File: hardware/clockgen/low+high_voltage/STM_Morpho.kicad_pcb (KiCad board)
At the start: 4 copper layers, 70 x 95.8 mm, 32 parts, among them CN10 Conn_02x19_Odd_Even, CN7 Conn_02x19_Odd_Even, J1 Conn_02x20_Odd_Even, J2 Conn_02x20_Odd_Even, U1 74ALVC164245DLG4, U10 CD40109BNSR, U2 74ALVC164245DLG4, U3 CD40109BNSR, U4 CD40109BNSR, U5 CD40109BNSR, U6 CD40109BNSR, U7 CD40109BNSR, U8 CD40109BNSR, U9 CD40109BNSR

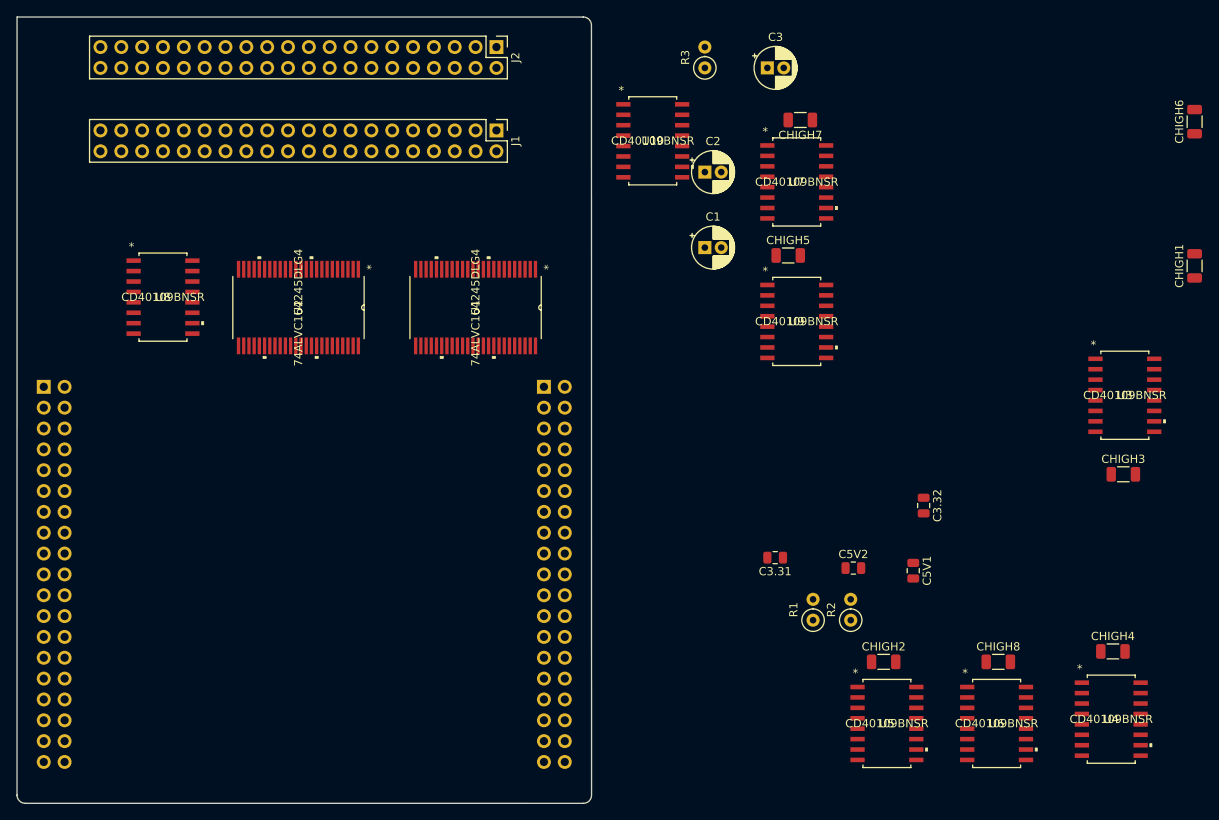
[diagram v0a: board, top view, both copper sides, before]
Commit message: Two PCBs are routed
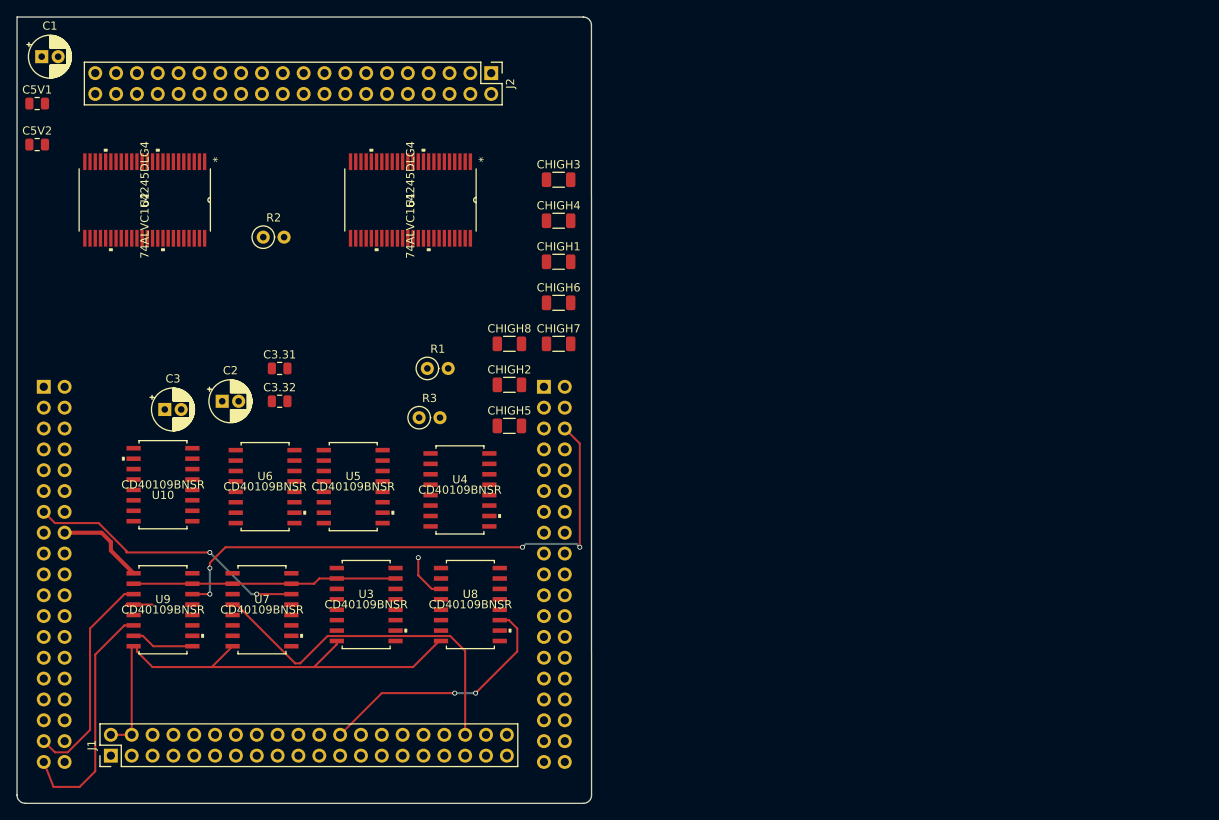
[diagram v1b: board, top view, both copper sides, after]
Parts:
- J1, J2: value Conn_02x20_Odd_Even -> Conn_02x20_Counter_Clockwise
- moved C5V1 121.0 mm to (132.4, 36.7), turned to 0 degrees
- moved C5V2 112.1 mm to (132.4, 41.7)
- moved U3 95.9 mm to (172.5, 97.8)
- moved U6 93.7 mm to (160.2, 83.4)
- moved J1 89.5 mm to (141.4, 116.2), turned to 90 degrees
- moved CHIGH4 85.6 mm to (196.0, 51.0)
- moved R2 85.5 mm to (160.0, 53.0), turned to 0 degrees
- moved U9 84.9 mm to (147.8, 98.4)
- moved C3 84.4 mm to (148.0, 74.0)
- moved U4 84.1 mm to (184.0, 83.8)
- moved C1 84.1 mm to (133.0, 31.0)
- moved U7 83.5 mm to (159.8, 98.4)
- moved CHIGH6 80.6 mm to (196.0, 61.0), turned to 0 degrees
- moved C3.32 79.5 mm to (162.0, 73.0), turned to 0 degrees
- moved CHIGH3 77.6 mm to (196.0, 46.0)
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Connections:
- CN10 pad 16: (no net) -> /PB12
- CN10 pad 22: (no net) -> /PB2
- CN10 pad 24: (no net) -> /PB1
- CN10 pad 26: (no net) -> /PB15
- CN10 pad 27: (no net) -> /PB4
- CN10 pad 28: (no net) -> /PB14
- CN10 pad 30: (no net) -> /PB13
- CN10 pad 31: (no net) -> /PB3
- CN10 pad 32: (no net) -> /AGND
- CN10 pad 7: (no net) -> /AVDD
- CN10 pad 8: (no net) -> /U5V
- CN7 pad 12: (no net) -> /IOREF
- CN7 pad 14: (no net) -> /RESET
- CN7 pad 2: (no net) -> /PC11
- CN7 pad 21: (no net) -> /PB7
- CN7 pad 23: (no net) -> /PC13
- CN7 pad 24: (no net) -> /VIN
- CN7 pad 25: (no net) -> /PC14
- CN7 pad 27: (no net) -> /PC15
- CN7 pad 29: (no net) -> /PH0
- CN7 pad 3: (no net) -> /PC12
- CN7 pad 31: (no net) -> /PH1
- CN7 pad 33: (no net) -> /VBAT
- CN7 pad 34: (no net) -> /PB0
- CN7 pad 4: (no net) -> /PD2
- CN7 pad 5: (no net) -> /VDD
- CN7 pad 6: (no net) -> /E5V
- CN7 pad 7: (no net) -> /BOOT0
- J1 pad 10: /PB9_5V -> /PC8_HIGH
- J1 pad 11: /PA6_5V -> /PB6_HIGH
- J1 pad 12: /PA7_5V -> /PC6_HIGH
- J1 pad 13: /PA1_5V -> /PA0_HIGH
- J1 pad 14: /PA2_5V -> /PC5_HIGH
- J1 pad 15: /PA3_5V -> /PC7_HIGH
- J1 pad 16: /PA4_5V -> /PC4_HIGH
- J1 pad 17: /PA5_5V -> /PB8_HIGH
- J1 pad 18: /PA8_5V -> /PC3_HIGH
- J1 pad 19: /NC -> /PB9_HIGH
- J1 pad 2: +3V3 -> GND
- J1 pad 20: /NC -> /PC2_HIGH
- J1 pad 21: GND -> /PA6_HIGH
- J1 pad 22: GND -> /PC1_HIGH
- J1 pad 23: /PA9_5V -> /PA7_HIGH
- J1 pad 24: /PA11_5V -> /PC0_HIGH
- J1 pad 25: /PA12_5V -> /PA1_HIGH
- J1 pad 26: /PA13_5V -> /PA15_HIGH
- J1 pad 27: /PA14_5V -> /PA2_HIGH
- J1 pad 28: /PA15_5V -> /PA14_HIGH
- J1 pad 29: /PC0_5V -> /PA3_HIGH
- J1 pad 3: /PA10_5V -> +3V3
- J1 pad 30: /PC1_5V -> /PA13_HIGH
- J1 pad 31: /PC2_5V -> /PA4_HIGH
- J1 pad 32: /PC3_5V -> /PA12_HIGH
- J1 pad 33: /PC4_5V -> /PA5_HIGH
- J1 pad 34: /PC5_5V -> /PA11_HIGH
- J1 pad 35: /PC6_5V -> /PA8_HIGH
- J1 pad 36: /PC8_5V -> /PA9_HIGH
- J1 pad 37: /PC9_5V -> +15V
- J1 pad 38: /PC10_5V -> GND
- J1 pad 39: GND -> +15V
- J1 pad 4: /PB10_5V -> GND
- J1 pad 5: /PB5_5V -> /PA10_HIGH
- J1 pad 6: /PB6_5V -> /PC10_HIGH
- J1 pad 7: /PA0_5V -> /PB10_HIGH
- J1 pad 8: /PC7_5V -> /PC9_HIGH
- J1 pad 9: /PB8_5V -> /PB5_HIGH
- J2 pad 10: /PB9_HIGH -> /PA12_5V
- J2 pad 11: /PA6_HIGH -> /PB6_5V
- J2 pad 12: /PA7_HIGH -> /PA13_5V
- J2 pad 13: /PA1_HIGH -> /PA0_5V
- J2 pad 14: /PA2_HIGH -> /PA14_5V
- J2 pad 15: /PA3_HIGH -> /PC7_5V
- J2 pad 16: /PA4_HIGH -> /PA15_5V
- J2 pad 17: /PA5_HIGH -> /PB8_5V
- J2 pad 18: /PA8_HIGH -> /PC0_5V
- J2 pad 19: +15V -> /PB9_5V
- J2 pad 2: +3V3 -> GND
- J2 pad 20: +15V -> /PC1_5V
- J2 pad 21: GND -> /PA6_5V
- J2 pad 22: GND -> /PC2_5V
- J2 pad 23: /PA9_HIGH -> /PA7_5V
- J2 pad 24: /PA11_HIGH -> /PC3_5V
- J2 pad 25: /PA12_HIGH -> /PA1_5V
- J2 pad 26: /PA13_HIGH -> /PC4_5V
- J2 pad 27: /PA14_HIGH -> /PA2_5V
- J2 pad 28: /PA15_HIGH -> /PC5_5V
- J2 pad 29: /PC0_HIGH -> /PA3_5V
- J2 pad 3: /PA10_HIGH -> +3V3
- J2 pad 30: /PC1_HIGH -> /PC6_5V
- J2 pad 31: /PC2_HIGH -> /PA4_5V
- J2 pad 32: /PC3_HIGH -> /PC8_5V
- J2 pad 33: /PC4_HIGH -> /PA5_5V
- J2 pad 34: /PC5_HIGH -> /PC9_5V
- J2 pad 35: /PC6_HIGH -> /PA8_5V
- J2 pad 36: /PC8_HIGH -> /PC10_5V
- J2 pad 37: /PC9_HIGH -> /NC
- J2 pad 38: /PC10_HIGH -> GND
- J2 pad 39: GND -> /NC
- J2 pad 4: /PB10_HIGH -> GND
- J2 pad 5: /PB5_HIGH -> /PA10_5V
- J2 pad 6: /PB6_HIGH -> /PA9_5V
- J2 pad 7: /PA0_HIGH -> /PB10_5V
- J2 pad 8: /PC7_HIGH -> /PA11_5V
- J2 pad 9: /PB8_HIGH -> /PB5_5V
- U10 pad 12: (no net) -> Net-(U10-Pad12)
- U3 pad 12: (no net) -> Net-(U3-Pad12)
- U4 pad 12: (no net) -> Net-(U4-Pad12)
- U5 pad 12: (no net) -> Net-(U5-Pad12)
- U6 pad 12: (no net) -> Net-(U6-Pad12)
- U7 pad 12: (no net) -> Net-(U7-Pad12)
- U8 pad 12: (no net) -> Net-(U8-Pad12)
- U9 pad 12: (no net) -> Net-(U9-Pad12)
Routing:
- net /PC5: track 0.00 -> 67.6 mm, vias 0 -> 4
- net GND: track 0.00 -> 61.5 mm
- net /PA9_HIGH: track 0.00 -> 43.7 mm
- net /PULLUP_HIGH: track 0.00 -> 40.3 mm
- net /PA13: track 0.00 -> 34.4 mm, vias 0 -> 2
- net /PC0_HIGH: track 0.00 -> 31.1 mm, vias 0 -> 2
- net /PC3: track 0.00 -> 29.5 mm
- net /PC2: track 0.00 -> 26.7 mm
- net +3V3: track 0.00 -> 11.1 mm
- net /PA14: track 0.00 -> 5.61 mm, vias 0 -> 1
- net /PC2_HIGH: track 0.00 -> 4.04 mm
